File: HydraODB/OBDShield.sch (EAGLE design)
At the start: 11 parts, among them IC1 7805L, J1 HYDRABUS_SHIELD_CON_HEADER_2X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, J2 HYDRABUS_SHIELD_CON_HEADER_2X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, J3 HYDRABUS_SHIELD_CON_HEADER_2X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, U2 SN65HVD233D

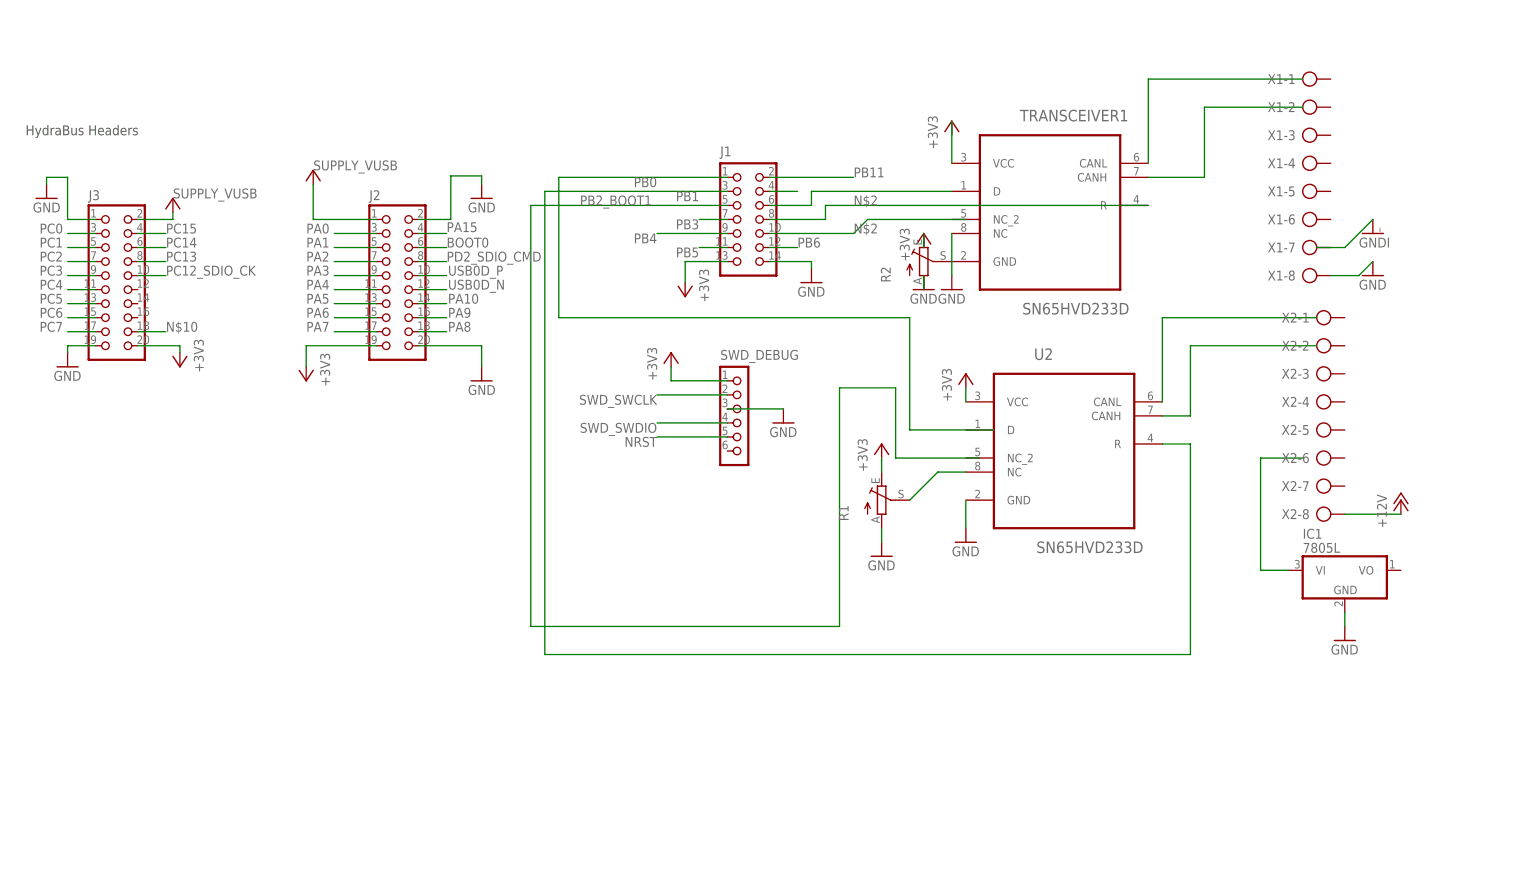
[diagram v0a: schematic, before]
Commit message: Rebuilt everything, schema and board were inconsistent. First try at PCB routing.
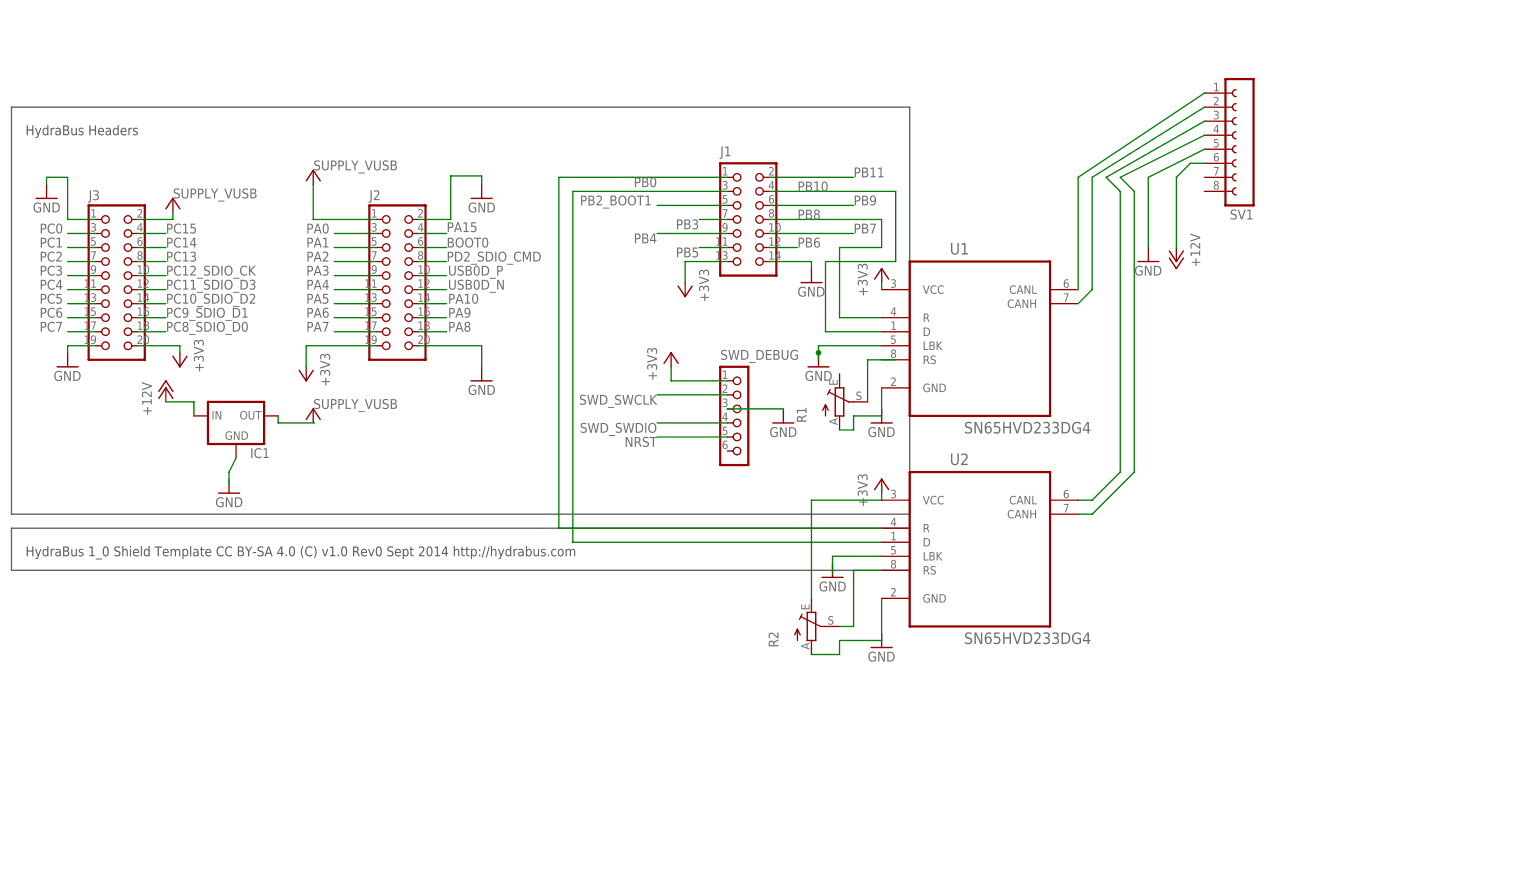
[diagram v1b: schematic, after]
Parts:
- removed TRANSCEIVER1: SN65HVD233D, Texas Instruments_By_element14_Batch_1:SN65HVD233D
- removed X1, X2: (no value), con-ptr500:AK300/8
- added SV1: (no value), con-lsta:FE08-1
- added U1: SN65HVD233DG4, Texas Instruments_By_element14_Batch_1:SN65HVD233DG4
- IC1: value 7805L -> (none); device linear:7805L -> v-reg:78XXS
- R1: device pot:TRIM_EU-S64W -> pot:TRIM_EU-B25U
- R2: device pot:TRIM_EU-S63S -> pot:TRIM_EU-B25U
- U2: value SN65HVD233D -> SN65HVD233DG4; device Texas Instruments_By_element14_Batch_1:SN65HVD233D -> Texas Instruments_By_element14_Batch_1:SN65HVD233DG4
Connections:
- net N$10 renamed PC8_SDIO_D0
- net N$2 renamed PB7
- removed net N$3: U2.CANL
- removed net N$5: TRANSCEIVER1.R
- removed net N$8: TRANSCEIVER1.CANL
- removed net PB1: J1.3, U2.R
- new net N$10: SV1.2, U1.CANH
- new net N$13: IC1.GND
- new net N$14: R2.A, U2.GND
- new net N$16: R1.S
- new net N$17: R2.S, U2.RS
- new net N$18: U2.LBK
- new net N$20: J1.3, U2.D
- new net PB8: J1.8, U1.R
- new net PB9: J1.6
- new net PC10_SDIO_D2: J3.14
- new net PC11_SDIO_D3: J3.12
- new net PC9_SDIO_D1: J3.16
- net +12V: now also IC1.IN, SV1.6; no longer X2-8.KL
- net +3V3: no longer R1.E, R2.E, U2.VCC
- net GND: now also SV1.5, U1.LBK; no longer IC1.GND, R1.A, R2.A, TRANSCEIVER1.GND, U2.GND, X1-8.KL
- net N$1: now also U1.VCC; no longer TRANSCEIVER1.VCC
- net N$11: now also SV1.3, U2.CANL; no longer U2.CANH
- net N$12: now also SV1.4, U2.CANH; no longer IC1.VI
- net N$4: now also IC1.OUT; no longer J1.6, TRANSCEIVER1.D
- net N$6: now also R2.E, U2.VCC; no longer R1.S, U2.NC
- net N$7: now also R1.A, U1.GND; no longer R2.S
- net N$9: now also SV1.1, U1.CANL; no longer TRANSCEIVER1.CANH
- net PB0: now also U2.R
- net PB10: now also U1.D
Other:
- note added: "HydraBus 1_0 Shield Template CC BY-SA 4.0 (C) v1.0 Rev0 Sept 2014 http://hydrabus.com"
- moved on the sheet: R1, R2, U2

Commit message: Placing and routing
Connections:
- removed net N$13: IC1.GND
- removed net N$14: R2.A, U2.GND
- removed net N$16: R1.S
- removed net N$18: U2.LBK
- removed net N$20: J1.3, U2.D
- removed net N$4: IC1.OUT
- removed net N$6: R2.E, U2.VCC
- removed net N$7: R1.A, U1.GND
- removed net PB0: J1.1, U2.R
- net +3V3: now also R1.E, R2.E, U1.VCC, U2.VCC
- net GND: now also IC1.GND, R1.A, R2.A, U1.GND, U2.GND, U2.LBK
- net N$1: now also R1.S, U1.RS; no longer U1.VCC
- net PB10: now also J1.6; no longer J1.4
- net PB11: now also J1.4, U2.D; no longer J1.2
- net PB9: now also J1.2, U2.R; no longer J1.6
- net VUSB: now also IC1.OUT
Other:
- note removed: "HydraBus 1_0 Shield Template CC BY-SA 4.0 (C) v1.0 Rev0 Sept 2014 http://hydrabus.com"
- note removed: "HydraBus Headers"
- moved on the sheet: R1, R2, SV1, U1, U2

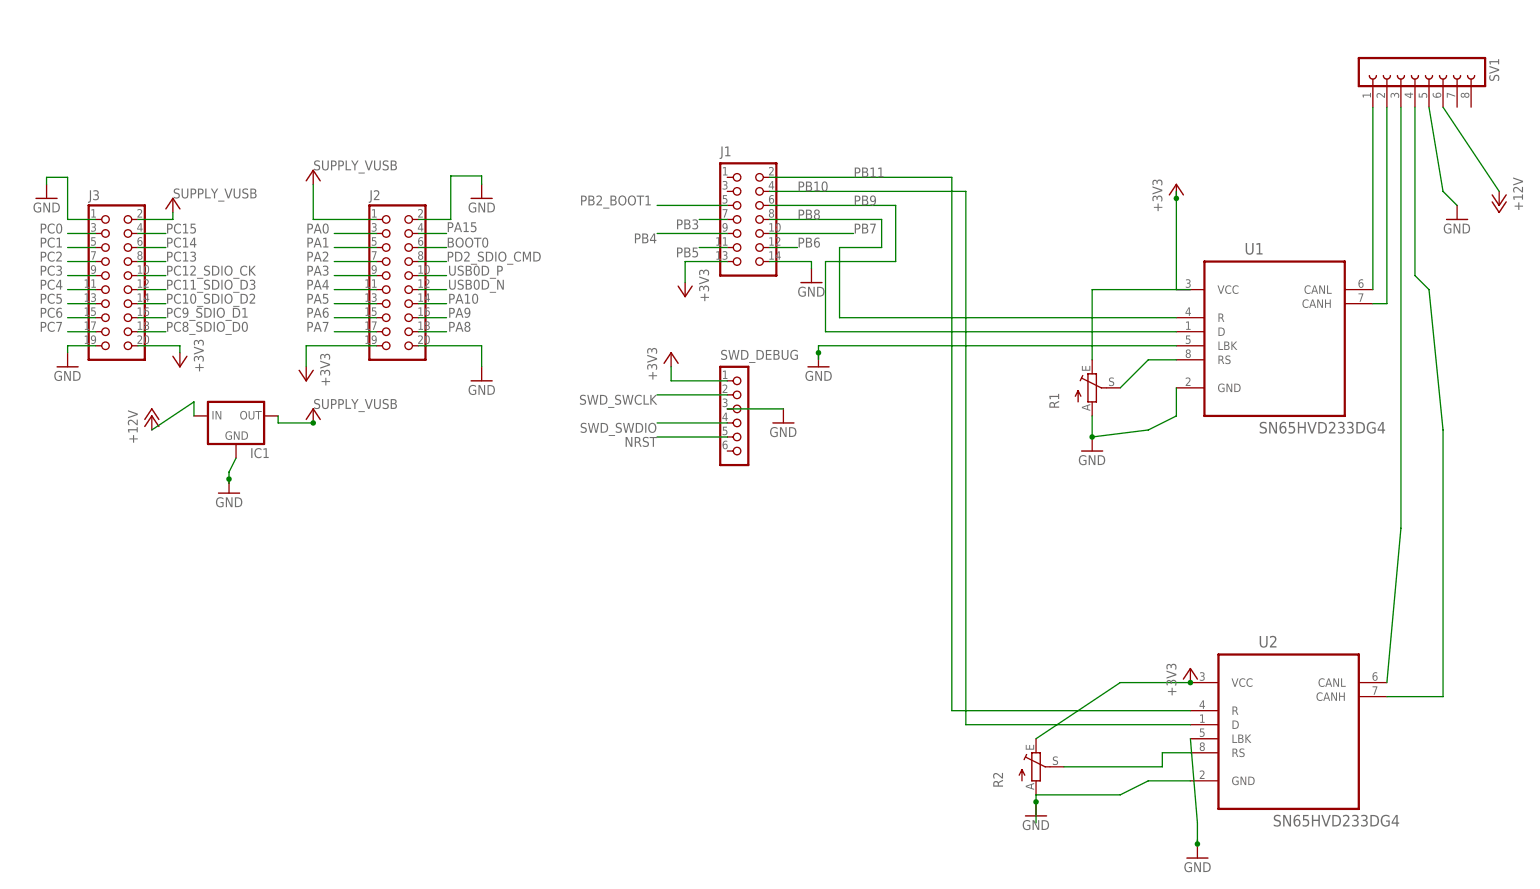
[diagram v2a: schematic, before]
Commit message: Proto pcb routing
Routing signle layer for proto pcb
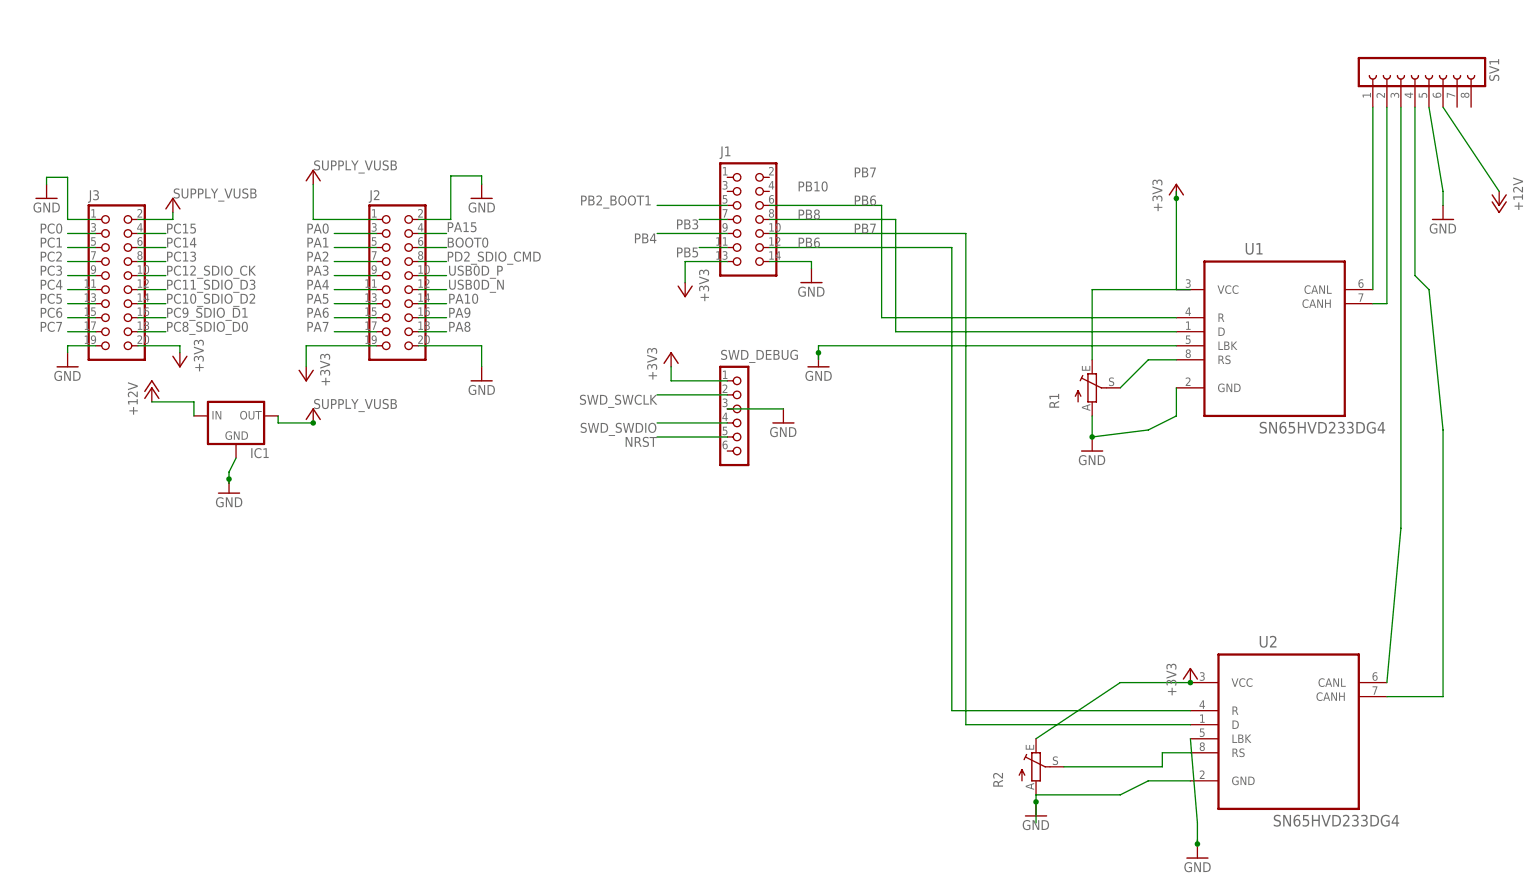
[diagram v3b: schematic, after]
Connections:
- removed net PB11: J1.4, U2.D
- removed net PB9: J1.2, U2.R
- net PB10: now also J1.8; no longer J1.6
- net PB6: now also U2.R
- net PB7: now also U2.D
- net PB8: now also J1.6; no longer J1.8
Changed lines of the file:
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@@
 <instance part="SV1" gate="G$1" x="200.66" y="154.94" rot="R270"/>
 <instance part="GND7" gate="1" x="-13.97" y="77.47" rot="MR0"/>
-<instance part="P+1" gate="1" x="-27.94" y="91.44"/>
+<instance part="P+1" gate="1" x="-27.94" y="96.52"/>
 <instance part="P+2" gate="1" x="215.9" y="129.54" rot="R180"/>
-<instance part="GND8" gate="1" x="208.28" y="127"/>
+<instance part="GND8" gate="1" x="205.74" y="127"/>
 <instance part="GND10" gate="1" x="132.08" y="19.05"/>
 <instance part="GND11" gate="1" x="92.71" y="100.33" rot="MR0"/>
@@
 <pinref part="GND8" gate="1" pin="GND"/>
 <pinref part="SV1" gate="G$1" pin="5"/>
-<wire x1="208.28" y1="129.54" x2="205.74" y2="132.08" width="0.1524" layer="91"/>
+<wire x1="205.74" y1="129.54" x2="205.74" y2="132.08" width="0.1524" layer="91"/>
 <wire x1="205.74" y1="132.08" x2="203.2" y2="147.32" width="0.1524" layer="91"/>
 </segment>
@@
 </segment>
 </net>
-<net name="PB11" class="0">
-<segment>
-<label x="99.06" y="134.62" size="1.778" layer="95"/>
-<pinref part="U2" gate="A" pin="D"/>
-<wire x1="160.02" y1="35.56" x2="119.38" y2="35.56" width="0.1524" layer="91"/>
-<wire x1="119.38" y1="35.56" x2="119.38" y2="132.08" width="0.1524" layer="91"/>
-<pinref part="J1" gate="J" pin="4"/>
-<wire x1="119.38" y1="132.08" x2="83.82" y2="132.08" width="0.1524" layer="91"/>
-</segment>
-</net>
 <net name="PB10" class="0">
 <segment>
 <label x="88.9" y="132.08" size="1.778" layer="95"/>
 <pinref part="U1" gate="A" pin="D"/>
-<wire x1="157.48" y1="106.68" x2="93.98" y2="106.68" width="0.1524" layer="91"/>
-<wire x1="93.98" y1="106.68" x2="93.98" y2="119.38" width="0.1524" layer="91"/>
-<wire x1="93.98" y1="119.38" x2="106.68" y2="119.38" width="0.1524" layer="91"/>
-<wire x1="106.68" y1="119.38" x2="106.68" y2="129.54" width="0.1524" layer="91"/>
-<pinref part="J1" gate="J" pin="6"/>
-<wire x1="106.68" y1="129.54" x2="83.82" y2="129.54" width="0.1524" layer="91"/>
+<wire x1="157.48" y1="106.68" x2="106.68" y2="106.68" width="0.1524" layer="91"/>
+<wire x1="106.68" y1="106.68" x2="106.68" y2="127" width="0.1524" layer="91"/>
+<pinref part="J1" gate="J" pin="8"/>
+<wire x1="83.82" y1="127" x2="106.68" y2="127" width="0.1524" layer="91"/>
 </segment>
 </net>
@@
 <segment>
 <label x="88.9" y="127" size="1.778" layer="95"/>
-<wire x1="104.14" y1="127" x2="104.14" y2="121.92" width="0.1524" layer="91"/>
-<wire x1="104.14" y1="121.92" x2="96.52" y2="121.92" width="0.1524" layer="91"/>
-<wire x1="96.52" y1="121.92" x2="96.52" y2="109.22" width="0.1524" layer="91"/>
+<wire x1="104.14" y1="129.54" x2="104.14" y2="109.22" width="0.1524" layer="91"/>
 <pinref part="U1" gate="A" pin="R"/>
-<wire x1="96.52" y1="109.22" x2="157.48" y2="109.22" width="0.1524" layer="91"/>
-<pinref part="J1" gate="J" pin="8"/>
-<wire x1="83.82" y1="127" x2="104.14" y2="127" width="0.1524" layer="91"/>
+<wire x1="104.14" y1="109.22" x2="157.48" y2="109.22" width="0.1524" layer="91"/>
+<pinref part="J1" gate="J" pin="6"/>
+<wire x1="104.14" y1="129.54" x2="83.82" y2="129.54" width="0.1524" layer="91"/>
 </segment>
 </net>
@@
 </segment>
 </net>
-<net name="PB7" class="0">
-<segment>
-<wire x1="83.82" y1="124.46" x2="99.06" y2="124.46" width="0.1524" layer="91"/>
-<label x="99.06" y="124.46" size="1.778" layer="95"/>
-<pinref part="J1" gate="J" pin="10"/>
-</segment>
-</net>
-<net name="PB6" class="0">
-<segment>
-<wire x1="83.82" y1="121.92" x2="88.9" y2="121.92" width="0.1524" layer="91"/>
-<label x="88.9" y="121.92" size="1.778" layer="95"/>
-<pinref part="J1" gate="J" pin="12"/>
-</segment>
-</net>
 <net name="PB5" class="0">
 <segment>
@@
 <wire x1="76.2" y1="95.25" x2="63.5" y2="95.25" width="0.1524" layer="91"/>
 <label x="63.5" y="95.25" size="1.778" layer="95" rot="R180"/>
-</segment>
-</net>
-<net name="PB9" class="0">
-<segment>
-<label x="99.06" y="129.54" size="1.778" layer="95"/>
-<pinref part="U2" gate="A" pin="R"/>
-<wire x1="160.02" y1="38.1" x2="116.84" y2="38.1" width="0.1524" layer="91"/>
-<wire x1="116.84" y1="38.1" x2="116.84" y2="134.62" width="0.1524" layer="91"/>
-<pinref part="J1" gate="J" pin="2"/>
-<wire x1="116.84" y1="134.62" x2="83.82" y2="134.62" width="0.1524" layer="91"/>
 </segment>
 </net>
@@
 <pinref part="P+1" gate="1" pin="+12V"/>
 <pinref part="IC1" gate="1" pin="IN"/>
-<wire x1="-27.94" y1="88.9" x2="-20.32" y2="93.98" width="0.1524" layer="91"/>
+<wire x1="-27.94" y1="93.98" x2="-20.32" y2="93.98" width="0.1524" layer="91"/>
 <wire x1="-20.32" y1="93.98" x2="-20.32" y2="91.44" width="0.1524" layer="91"/>
 </segment>
@@
 </segment>
 </net>
+<net name="PB6" class="0">
+<segment>
+<label x="99.06" y="129.54" size="1.778" layer="95"/>
+<pinref part="U2" gate="A" pin="R"/>
+<wire x1="160.02" y1="38.1" x2="116.84" y2="38.1" width="0.1524" layer="91"/>
+<wire x1="116.84" y1="38.1" x2="116.84" y2="121.92" width="0.1524" layer="91"/>
+<label x="88.9" y="121.92" size="1.778" layer="95"/>
+<pinref part="J1" gate="J" pin="12"/>
+<wire x1="116.84" y1="121.92" x2="83.82" y2="121.92" width="0.1524" layer="91"/>
+</segment>
+</net>
+<net name="PB7" class="0">
+<segment>
+<label x="99.06" y="134.62" size="1.778" layer="95"/>
+<pinref part="U2" gate="A" pin="D"/>
+<wire x1="160.02" y1="35.56" x2="119.38" y2="35.56" width="0.1524" layer="91"/>
+<wire x1="119.38" y1="35.56" x2="119.38" y2="124.46" width="0.1524" layer="91"/>
+<label x="99.06" y="124.46" size="1.778" layer="95"/>
+<pinref part="J1" gate="J" pin="10"/>
+<wire x1="119.38" y1="124.46" x2="83.82" y2="124.46" width="0.1524" layer="91"/>
+</segment>
+</net>
